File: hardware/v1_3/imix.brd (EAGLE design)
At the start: 87 x 102.5 mm, 151 parts, among them J2_3_5_AND_6 ARDUINO_R3NO_HOLES, Q2 AO3415, Q3 AO3415, Q4 AO3415, Q5 AO3415, U1 BQ2423X, U10 ISL29035, U11 FX0S8700CQ, U12 296-12686-1-ND, U3 TLV3202, U4 LM358, U5 LDO-TPS78233, U6 ATSAM4LCX_100, U8 SI7021, U9 NRF51422, X1 16MHz, X2 16MHz, X3 16MHz

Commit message: Update to most recent changeset for 1.3
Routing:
- net USART2_CLK: track 83.5 -> 74.9 mm, vias 5 -> 4
- net GND: track 219.8 -> 219.1 mm
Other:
- board text removed: "R27"
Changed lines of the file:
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@@
 <layers>
 <layer number="1" name="Top" color="4" fill="1" visible="yes" active="yes"/>
-<layer number="2" name="Route2" color="1" fill="3" visible="no" active="yes"/>
+<layer number="2" name="Route2" color="1" fill="3" visible="yes" active="yes"/>
 <layer number="3" name="Route3" color="4" fill="3" visible="no" active="no"/>
 <layer number="4" name="Route4" color="1" fill="4" visible="no" active="no"/>
@@
 <layer number="151" name="HeatSink" color="7" fill="1" visible="no" active="yes"/>
 <layer number="152" name="_bDocu" color="7" fill="1" visible="no" active="yes"/>
-<layer number="153" name="FabDoc1" color="15" fill="1" visible="yes" active="yes"/>
+<layer number="153" name="FabDoc1" color="15" fill="1" visible="no" active="yes"/>
 <layer number="154" name="FabDoc2" color="15" fill="1" visible="no" active="yes"/>
 <layer number="155" name="FabDoc3" color="7" fill="1" visible="no" active="yes"/>
@@
 <wire x1="52.1" y1="23.6" x2="49.7" y2="26" width="0.1524" layer="153"/>
 <wire x1="49.7" y1="26" x2="47.3" y2="23.6" width="0.1524" layer="153"/>
-<wire x1="53" y1="23.2" x2="55" y2="23.20710625" width="0.1524" layer="153"/>
-<wire x1="55" y1="23.20710625" x2="55" y2="19.671571875" width="0.1524" layer="153"/>
-<wire x1="55" y1="19.671571875" x2="53" y2="19.7" width="0.1524" layer="153"/>
-<wire x1="53" y1="19.7" x2="53" y2="23.2" width="0.1524" layer="153"/>
 <wire x1="57.3" y1="20.5" x2="57.3" y2="22.5" width="0.1524" layer="153"/>
 <wire x1="57.3" y1="22.5" x2="57.3" y2="24.5" width="0.1524" layer="153"/>
@@
 <text x="48.5" y="21.5" size="1.2" layer="153" font="vector" ratio="10" rot="R135">C26</text>
 <text x="46.9" y="19.9" size="1.2" layer="153" font="vector" ratio="10" rot="R135">C28</text>
-<text x="53.5" y="23.2" size="1.2" layer="153" font="vector" ratio="10" rot="R270">R27</text>
 <text x="42.2" y="23.7" size="1.2" layer="153" font="vector" ratio="10" rot="R135">C24</text>
 <text x="39.7" y="26.2" size="1.2" layer="153" font="vector" ratio="10" rot="R135">C23</text>
@@
 <circle x="33.23" y="65.28" radius="1.562046875" width="0.3" layer="153"/>
 <circle x="33.26" y="4.56" radius="1.562046875" width="0.3" layer="153"/>
-<circle x="81.98" y="-11.93" radius="1.562046875" width="0.3" layer="153"/>
+<circle x="82.48" y="-11.93" radius="1.562046875" width="0.3" layer="153"/>
 <circle x="82.5" y="46" radius="1.562046875" width="0.3" layer="153"/>
 <circle x="41.7" y="3.2" radius="1.140175" width="0.3" layer="153"/>
@@
 <circle x="45.3" y="8.3" radius="0.4242625" width="0.3" layer="154"/>
 <circle x="82.5" y="46" radius="1.562046875" width="0.3" layer="154"/>
-<circle x="82" y="-11.9" radius="1.562046875" width="0.3" layer="154"/>
+<circle x="82.6" y="-12" radius="1.562046875" width="0.3" layer="154"/>
 <wire x1="66" y1="72.5" x2="66" y2="78" width="0.1524" layer="153"/>
 <wire x1="66" y1="78" x2="74.7" y2="78" width="0.1524" layer="153"/>
@@
 <contactref element="U9" pad="5"/>
 <wire x1="55.9393375" y1="45.045940625" x2="54.985278125" y2="46" width="0.1524" layer="1"/>
-<wire x1="54.985278125" y1="46" x2="52" y2="46" width="0.1524" layer="1"/>
-<via x="52" y="46" extent="1-16" drill="0.3302"/>
 <wire x1="60.1" y1="3.9" x2="60.1" y2="6.1" width="0.1524" layer="1"/>
 <wire x1="66.25" y1="11.25" x2="66.25" y2="19.25" width="0.1524" layer="1"/>
@@
 <via x="55" y="46" extent="1-16" drill="0.3302"/>
 <contactref element="J2" pad="9"/>
-<wire x1="52" y1="46" x2="52" y2="51.5" width="0.1524" layer="16"/>
-<wire x1="52" y1="51.5" x2="57.58" y2="57.08" width="0.1524" layer="16"/>
-<wire x1="57.58" y1="57.08" x2="57.57" y2="57.09" width="0.1524" layer="16"/>
-<wire x1="57.57" y1="57.09" x2="57.57" y2="57.26" width="0.1524" layer="16"/>
 <wire x1="66.25" y1="19.25" x2="68.5" y2="21.5" width="0.1524" layer="1"/>
 <wire x1="68.5" y1="21.5" x2="68.5" y2="22" width="0.1524" layer="1"/>
+<wire x1="57.5" y1="49.25" x2="57.57" y2="49.32" width="0.1524" layer="16"/>
+<wire x1="57.57" y1="49.32" x2="57.57" y2="57.26" width="0.1524" layer="16"/>
 </signal>
 <signal name="USART2_RX">
@@
 <via x="73.81" y="-2.5" extent="1-16" drill="0.3302"/>
 <wire x1="46.0034" y1="28.746040625" x2="45.89895625" y2="29.101040625" width="0.1524" layer="1"/>
-<via x="45.5" y="26.5" extent="1-16" drill="0.3302"/>
+<via x="45.5" y="26.9" extent="1-16" drill="0.3302"/>
 <wire x1="49.575378125" y1="32.31801875" x2="47" y2="29.742640625" width="0.1524" layer="1"/>
 <wire x1="47" y1="29.742640625" x2="47" y2="29.5" width="0.1524" layer="1"/>
 <wire x1="47" y1="29.5" x2="46.5" y2="29.5" width="0.1524" layer="1"/>
-<wire x1="46.5" y1="29.5" x2="45" y2="28" width="0.1524" layer="1"/>
-<wire x1="45" y1="28" x2="45.5" y2="27.5" width="0.1524" layer="1"/>
-<wire x1="45.5" y1="27.5" x2="45.5" y2="26.5" width="0.1524" layer="1"/>
 <via x="59.25" y="33.25" extent="1-16" drill="0.3302"/>
 <via x="41.75" y="19.5" extent="1-16" drill="0.3302"/>
@@
 <wire x1="81.94" y1="82.885" x2="82.825" y2="82" width="0.4064" layer="1"/>
 <wire x1="82.825" y1="82" x2="83.5" y2="82" width="0.4064" layer="1"/>
+<wire x1="45.5" y1="26.9" x2="45.5" y2="28.6" width="0.1524" layer="1"/>
+<wire x1="45.5" y1="28.6" x2="46.5" y2="29.5" width="0.1524" layer="1"/>
 </signal>
 <signal name="SWDIO/TMS">

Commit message: Add 1K resistor b/n FTDI DTR and RESET. Closes #15
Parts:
- added R8: 1K, imix:0603-RES
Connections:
- new net DTR: J1.15, R8.2, U7.18
- net !RESET: now also R8.1; no longer J1.15, U7.18
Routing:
- net !RESET: track 147.9 -> 127.4 mm, vias 7 -> 5
- net DTR: track 0.00 -> 18.8 mm, vias 0 -> 2
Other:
- board text added: "IMIX v1.3 2/17 Shane Leonard"
- board text added: "IMIX v1.3 Feb 2017 Shane Leonard"
- board text added: "R8"
- board text removed: "IMIX v1.2 11/16 Shane Leonard"
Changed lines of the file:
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@@
 <layer number="151" name="HeatSink" color="7" fill="1" visible="no" active="yes"/>
 <layer number="152" name="_bDocu" color="7" fill="1" visible="no" active="yes"/>
-<layer number="153" name="FabDoc1" color="15" fill="1" visible="no" active="yes"/>
-<layer number="154" name="FabDoc2" color="15" fill="1" visible="no" active="yes"/>
+<layer number="153" name="FabDoc1" color="15" fill="1" visible="yes" active="yes"/>
+<layer number="154" name="FabDoc2" color="15" fill="1" visible="yes" active="yes"/>
 <layer number="155" name="FabDoc3" color="7" fill="1" visible="no" active="yes"/>
 <layer number="199" name="Contour" color="7" fill="1" visible="no" active="yes"/>
@@
 <wire x1="33.594878125" y1="0" x2="0" y2="0" width="0.1524" layer="20"/>
 <text x="18" y="11.75" size="1.016" layer="21" font="vector" ratio="12">PWR MEAS</text>
-<text x="56.7" y="-9.65" size="1.4224" layer="21" font="vector" ratio="12" rot="R180">IMIX v1.2 11/16
+<text x="56.7" y="-9.65" size="1.4224" layer="21" font="vector" ratio="12" rot="R180">IMIX v1.3 2/17
 Shane Leonard</text>
 <text x="53.5" y="46.5" size="1.27" layer="21" font="vector" ratio="12" rot="R225">ATSAM4LC8</text>
@@
 <dimension x1="0" y1="70" x2="37.5" y2="70" x3="18.75" y3="79" textsize="1.9304" layer="153" unit="inch" precision="3" visible="yes"/>
 <text x="5" y="11" size="1.2" layer="153" font="vector">BATT CLIP</text>
-<text x="-16.5" y="-36" size="2.54" layer="153" font="vector">IMIX v1.2 Oct 2016
+<text x="-16.5" y="-36" size="2.54" layer="153" font="vector">IMIX v1.3 Feb 2017
 Shane Leonard</text>
 <wire x1="48" y1="74.8" x2="49" y2="74.8" width="0.1524" layer="153"/>
@@
 <hole x="82.5" y="-12" drill="3"/>
 <hole x="82.5" y="46" drill="3"/>
+<wire x1="16.05" y1="25.45" x2="14.35" y2="25.45" width="0.1" layer="22"/>
+<wire x1="14.35" y1="25.45" x2="14.35" y2="22.05" width="0.1" layer="22"/>
+<wire x1="16.05" y1="25.45" x2="16.05" y2="22.05" width="0.1" layer="22"/>
+<wire x1="16.05" y1="22.05" x2="14.35" y2="22.05" width="0.1" layer="22"/>
+<text x="13.23" y="23.19" size="0.762" layer="22" font="vector" ratio="10" rot="MR90">R8</text>
+<text x="14.7" y="22.9" size="1.2" layer="154" font="vector" ratio="10" rot="MR90">R8</text>
+<wire x1="16.1" y1="22" x2="16.1" y2="25.5" width="0.1524" layer="154"/>
+<wire x1="14.3" y1="25.5" x2="16.1" y2="25.5" width="0.1524" layer="154"/>
+<wire x1="14.3" y1="22" x2="14.3" y2="25.5" width="0.1524" layer="154"/>
+<wire x1="14.3" y1="22" x2="16.1" y2="22" width="0.1524" layer="154"/>
 </plain>
 <attributes>
@@
 <element name="C8" library="imix" package="C0603" value="4.7uF" x="13.5" y="48.5" rot="R270"/>
 <element name="R7" library="imix" package="0603-RES" value="10K" x="32" y="27" rot="R90"/>
+<element name="R8" library="imix" package="0603-RES" value="1K" x="15.2" y="23.8" rot="MR90"/>
 </elements>
 <signals>
@@
 <contactref element="J2_3_5_AND_6" pad="RESET@2"/>
 <via x="15.2" y="19.2" extent="1-16" drill="0.3302"/>
-<via x="15.2" y="28" extent="1-16" drill="0.3302"/>
 <wire x1="51.696696875" y1="30.196696875" x2="51" y2="29.5" width="0.1524" layer="1"/>
 <wire x1="51" y1="29.5" x2="51" y2="28.25" width="0.1524" layer="1"/>
@@
 <wire x1="51.25" y1="11.5" x2="51.42" y2="11.5" width="0.1524" layer="1"/>
 <wire x1="51.42" y1="11.5" x2="51.46" y2="11.54" width="0.1524" layer="1"/>
-<contactref element="J1" pad="15"/>
-<contactref element="U7" pad="18"/>
 <wire x1="28.5" y1="13" x2="18.4" y2="13" width="0.1524" layer="1"/>
 <wire x1="18.4" y1="13" x2="15.2" y2="16.2" width="0.1524" layer="1"/>
@@
 <wire x1="24.614" y1="7.975" x2="26.239" y2="7.98" width="0.1524" layer="1"/>
 <wire x1="26.239" y1="7.98" x2="27.5" y2="6.85" width="0.1524" layer="1"/>
-<wire x1="14" y1="33.6" x2="13.9" y2="33.5" width="0.1524" layer="16"/>
-<wire x1="15.9" y1="33.6" x2="14" y2="33.6" width="0.1524" layer="16"/>
-<wire x1="17" y1="32.5" x2="15.9" y2="33.6" width="0.1524" layer="16"/>
-<wire x1="13.9" y1="33.5" x2="13.85" y2="33.5" width="0.1524" layer="16"/>
-<wire x1="17" y1="35.4" x2="17.5" y2="35.9" width="0.1524" layer="1"/>
-<wire x1="17" y1="32.5" x2="17" y2="35.4" width="0.1524" layer="1"/>
-<via x="17" y="32.5" extent="1-16" drill="0.3302"/>
-<wire x1="17.5" y1="35.9" x2="20.08" y2="35.9" width="0.1524" layer="1"/>
-<wire x1="20.08" y1="35.9" x2="20.33" y2="35.65" width="0.1524" layer="1"/>
-<wire x1="15.2" y1="19.2" x2="15.2" y2="28" width="0.1524" layer="16"/>
-<wire x1="15.2" y1="28" x2="15.2" y2="29.2" width="0.1524" layer="1"/>
-<wire x1="15.2" y1="29.2" x2="17" y2="31" width="0.1524" layer="1"/>
-<wire x1="17" y1="31" x2="17" y2="32.5" width="0.1524" layer="1"/>
+<contactref element="R8" pad="1"/>
+<wire x1="15.2" y1="22.95" x2="15.2" y2="19.2" width="0.1524" layer="16"/>
 </signal>
 <signal name="SCK">
@@
 <wire x1="21.6" y1="29.3" x2="19.8" y2="29.3" width="0.1524" layer="1"/>
 </signal>
+<signal name="DTR">
+<contactref element="J1" pad="15"/>
+<contactref element="U7" pad="18"/>
+<contactref element="R8" pad="2"/>
+<wire x1="13.85" y1="33.5" x2="13.9" y2="33.5" width="0.1524" layer="16"/>
+<wire x1="20.33" y1="35.65" x2="20.08" y2="35.9" width="0.1524" layer="1"/>
+<wire x1="20.08" y1="35.9" x2="17.5" y2="35.9" width="0.1524" layer="1"/>
+<wire x1="17.5" y1="35.9" x2="17" y2="35.4" width="0.1524" layer="1"/>
+<wire x1="17" y1="35.4" x2="17" y2="32.5" width="0.1524" layer="1"/>
+<wire x1="17" y1="32.5" x2="17" y2="31" width="0.1524" layer="1"/>
+<wire x1="17" y1="31" x2="15.2" y2="29.2" width="0.1524" layer="1"/>
+<wire x1="15.2" y1="29.2" x2="15.2" y2="28" width="0.1524" layer="1"/>
+<wire x1="13.9" y1="33.5" x2="14" y2="33.6" width="0.1524" layer="16"/>
+<wire x1="14" y1="33.6" x2="15.9" y2="33.6" width="0.1524" layer="16"/>
+<wire x1="15.9" y1="33.6" x2="17" y2="32.5" width="0.1524" layer="16"/>
+<via x="17" y="32.5" extent="1-16" drill="0.3302"/>
+<via x="15.2" y="28" extent="1-16" drill="0.3302"/>
+<wire x1="15.2" y1="28" x2="15.2" y2="24.65" width="0.1524" layer="16"/>
+</signal>
 </signals>

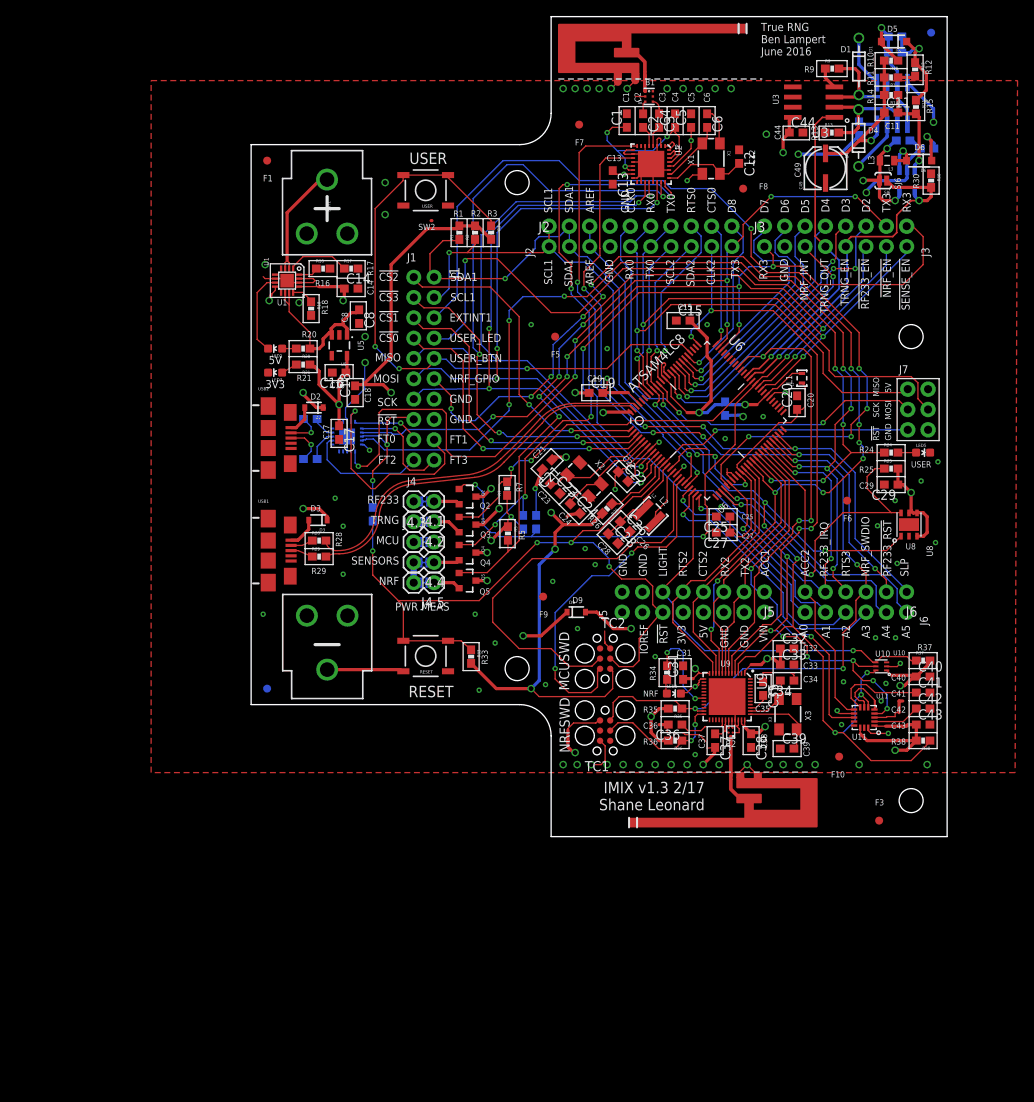
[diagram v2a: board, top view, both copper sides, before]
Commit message: Fix power bugs and other issues in schematic
* Set EN1 on the battery charger to VCC
* Replaced the PMOS load switches with SIP32041As
* Added isolation for the I2C and the RF233 SPI busses
* Connected the I2C pullups to VCC_MCU, not VCC_SENSE
* Added resistor between FTDI DTR and RESET (previous commit)
* Moved power sense headers logically inward towards their power domains
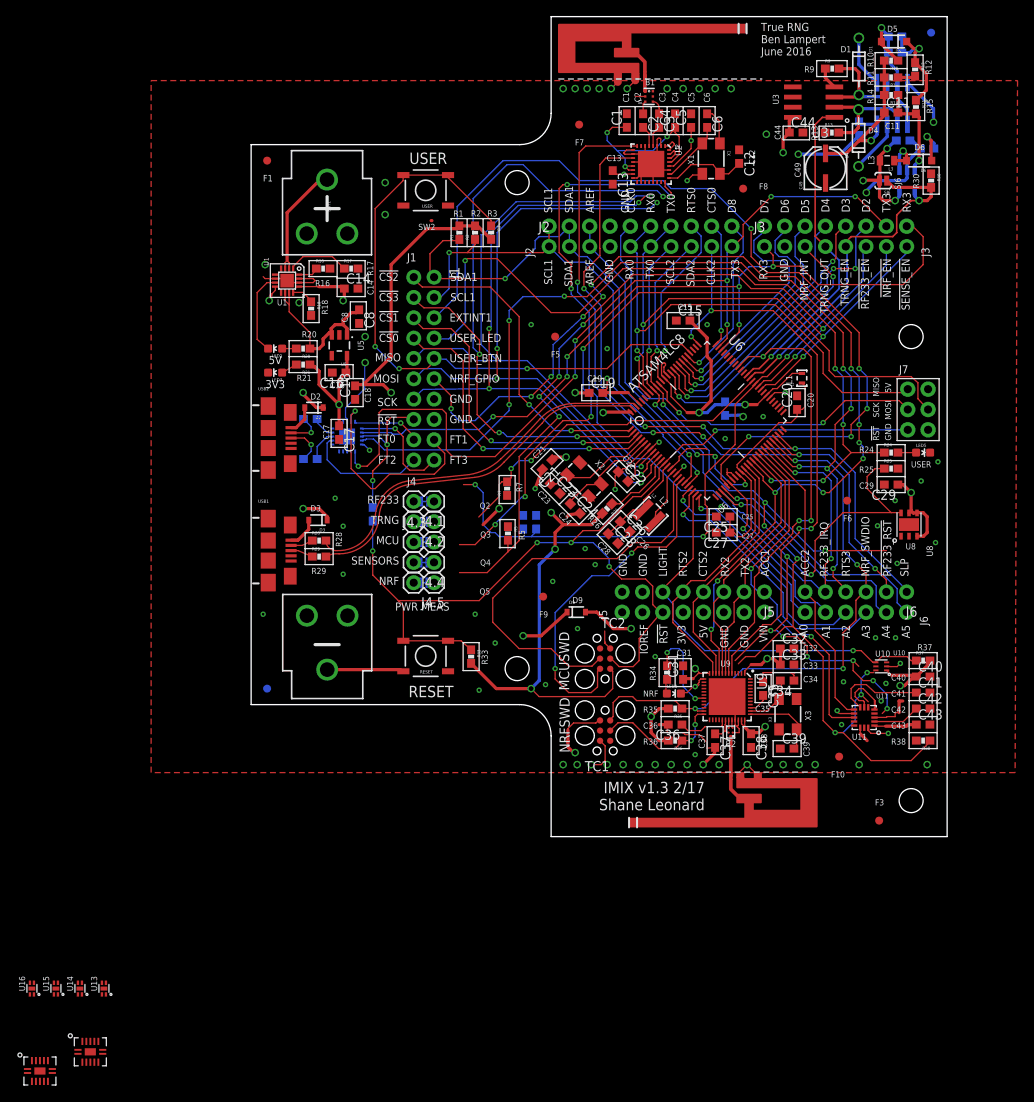
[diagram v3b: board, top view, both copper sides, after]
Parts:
- removed Q2, Q3, Q4, Q5: AO3415, SparkFun-DiscreteSemi:SOT23-3
- added U13, U14, U15, U16: SIP32401A, shaneleonard-master-lbr:TDFN4
- added U17, U18: 74LVC4066BQ, shaneleonard-master-lbr:DHVQFN14
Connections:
- removed net !NRF_PWR_EN: J3.7, Q5.1, R5.2, U6.60
- removed net !RF233_PWR_EN: J3.6, Q2.1, R6.2, U6.61
- removed net !SENSE_PWR_EN: J3.8, Q4.1, R4.2, U6.59
- removed net !TRNG_PWR_EN: Q3.1, R7.2, U6.62
- removed net N$14: J4.2.1, Q3.2, SJ7.2
- removed net N$36: J4.5.1, Q5.2, SJ2.2
- removed net N$37: J4.1.1, Q2.2, SJ3.2
- new net N$32: J4.2.1, SJ7.1, U16.1
- new net N$33: J4.1.1, SJ3.1, U15.1
- new net N$8: J4.4.1, SJ1.2, U13.1
- new net NRF_PWR_EN: J3.7, R5.2, U14.4, U18.13, U18.5, U6.60
- new net NRF_TWI_SCL: U18.3, U9.4
- new net NRF_TWI_SDA: U18.2, U9.3
- new net RF233_CS: U17.10, U2.23
- new net RF233_MISO: U17.2, U2.20
- new net RF233_MOSI: U17.3, U2.22
- new net RF233_PWR_EN: J3.6, R6.2, U15.4, U17.12, U17.13, U17.5, U17.6, U6.61
- new net RF233_SCK: U17.9, U2.19
- new net SENSE_PWR_EN: J3.8, R4.2, U13.4, U18.12, U18.6, U6.59
- new net SENSE_TWI_SCL: U10.5, U11.4, U18.10, U8.6
- new net SENSE_TWI_SDA: U10.6, U11.6, U18.9, U8.1
- new net TRNG_PWR_EN: R7.2, U16.4, U6.62
- net GND: now also R4.1, R5.1, R7.1, U13.2, U13.PADDLE, U14.2, U14.PADDLE, U15.2, U15.PADDLE, U16.2, U16.PADDLE, U17.7, U17.PADDLE, U18.7, U18.PADDLE
- net MISO: now also U17.1; no longer U2.20
- net MOSI: now also U17.4; no longer U2.22
- net N$18: now also J4.5.1, SJ2.1, U14.1; no longer J4.4.1, Q4.2, SJ1.2
- net SCK: now also U17.8; no longer U2.19
- net SPI_NCS3: now also U17.11; no longer U2.23
- net TWI2_SCL: now also U18.11, U18.4; no longer U10.5, U11.4, U8.6, U9.4
- net TWI2_SDA: now also U18.1, U18.8; no longer U10.6, U11.6, U8.1, U9.3
- net VCC_3V3: now also U13.3, U14.3, U15.3, U16.3; no longer J4.1.2, J4.2.2, J4.4.2, J4.5.2, R4.1, R5.1, R7.1, SJ1.1, SJ2.1, SJ3.1, SJ7.1
- net VCC_MCU_3V3: now also R25.2, R38.2, U17.14, U18.14
- net VCC_NRF_3V3: no longer Q5.3
- net VCC_RF233_3V3: now also J4.1.2, J4.5.2, SJ2.2, SJ3.2; no longer Q2.3
- net VCC_SENSE_3V3: now also J4.4.2, SJ1.1; no longer Q4.3, R25.2, R38.2
- net VCC_TRNG_3V3: now also J4.2.2, SJ7.2; no longer Q3.3
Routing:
- net !NRF_PWR_EN: track 103.1 -> 0.00 mm, vias 6 -> 0
- net NRF_PWR_EN: track 0.00 -> 103.0 mm, vias 0 -> 6
- net !SENSE_PWR_EN: track 98.6 -> 0.00 mm, vias 6 -> 0
- net SENSE_PWR_EN: track 0.00 -> 96.5 mm, vias 0 -> 6
- net !RF233_PWR_EN: track 82.2 -> 0.00 mm, vias 3 -> 0
- net RF233_PWR_EN: track 0.00 -> 81.4 mm, vias 0 -> 3
- net VCC_3V3: track 95.5 -> 23.9 mm, vias 4 -> 2
- net VCC_SENSE_3V3: track 90.6 -> 27.0 mm, vias 4 -> 2
- net VCC_RF233_3V3: track 67.5 -> 9.05 mm, vias 3 -> 2
- net !TRNG_PWR_EN: track 45.3 -> 0.00 mm, vias 2 -> 0
- net TRNG_PWR_EN: track 0.00 -> 42.8 mm, vias 0 -> 2
- net VCC_NRF_3V3: track 47.1 -> 32.4 mm, vias 6 -> 5
- net TWI2_SDA: track 132.4 -> 127.5 mm
- net TWI2_SCL: track 120.9 -> 116.1 mm
- net N$14: track 4.39 -> 0.00 mm
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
